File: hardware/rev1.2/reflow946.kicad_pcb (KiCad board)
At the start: 2 copper layers, 104 x 60 mm, 56 parts, among them J1 VH-2A, J2 VH-3A2, J3 VH-3A2, J4 XH-A2, J5 HDR-M-2.54_2x3, Q1 BTA16-600BRG, Q2 MMBT3906, Q3 MMBT3906, Q4 MMBT3906, SW1 SW_Push, SW2 SW_Push, SW3 SW_Push, U1 MOC3041M, U2 ESP32-WROOM-32U, U3 MAX31855KASA, U4 AMS1117-3.3

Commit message: Fork to randware R2 variant
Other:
- board text added: "r2"
- board text added: "randware.us"
- board text removed: "Arnaud Durand"
- board text removed: "r1.2"

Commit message: pcb rev2: place all new parts, TFT alignment silk, pogo-pad J6
- J6: custom 8x SMD pogo-pad array (dia1.6, 2.54 pitch) at bottom strip
  (inside-window THT header rejected: 11.5mm body clashes display glass;
  original location shorted existing segment copper)
- U6/C7/FB3/FB4 probe cluster center field; J7 header top strip;
  J8 EXT_TC terminal bottom-left beside factory probe conn J4
- R21/R22 relocated clear of Reflow946 branding and +3.3V rail track
- Silk: ST7789V3 alignment boxes (32.4x17.3 active / 36x19.3 glass),
  fiducial crosshairs, CC BY 4.0 attribution line
- Zones refilled; DRC vs baseline: zero new electrical/courtyard/mask
  violations; remaining = silk cosmetics + 15 unrouted new-net pads
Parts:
- added C7: 0.01u, C_0805_2012Metric_Pad1.18x1.45mm_HandSolder, F.Cu at (144.0, 105.5)
- added FB3: FerriteBead, R_0603_1608Metric_Pad0.98x0.95mm_HandSolder, F.Cu at (155.5, 103.8)
- added FB4: FerriteBead, R_0603_1608Metric_Pad0.98x0.95mm_HandSolder, F.Cu at (155.5, 107.2)
- added J6: TFT_POGO, , F.Cu at (142.6, 124.3)
- added J7: PROBE_BRK, PinHeader_1x06_P2.54mm_Vertical, F.Cu at (156.0, 74.5)
- added J8: EXT_TC, TerminalBlock_Phoenix_MPT-0,5-2-2.54_1x02_P2.54mm_Horizontal, F.Cu at (108.3, 125.9)
- added R21: 4.7k, R_0603_1608Metric_Pad0.98x0.95mm_HandSolder, F.Cu at (132.5, 119.5)
- added R22: 4.7k, R_0603_1608Metric_Pad0.98x0.95mm_HandSolder, F.Cu at (132.5, 123.2)
- added U6: MAX31855KASA, SOIC-8_3.9x4.9mm_P1.27mm, F.Cu at (150.0, 105.5)
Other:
- board text added: "Based on Reflow946 by A. Durand | CC BY 4.0"
- board text added: "J6"
- board text added: "ST7789V3 ALIGN 32.4x17.3"

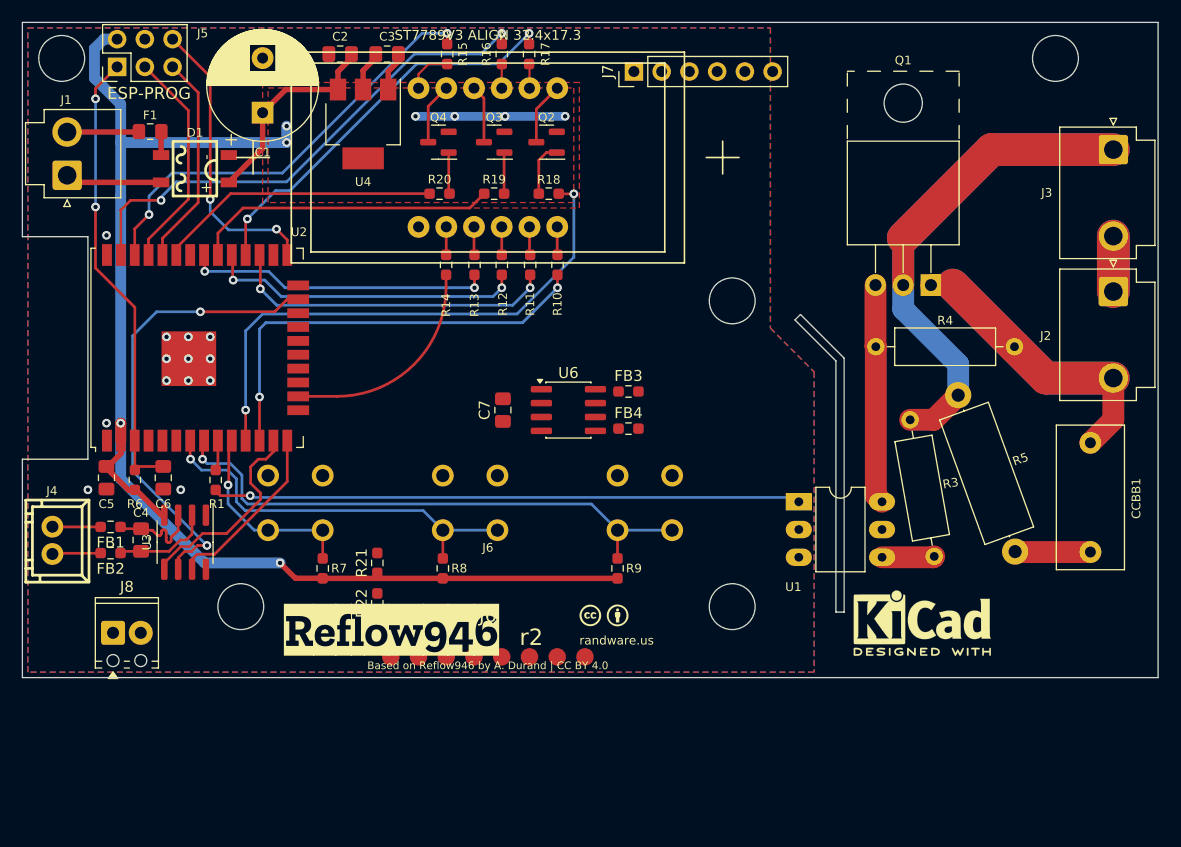
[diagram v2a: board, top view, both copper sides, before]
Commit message: rev2: remove I2C expansion pull-ups R21/R22 (vestigial — display went SPI; IO17/IO22 spare)
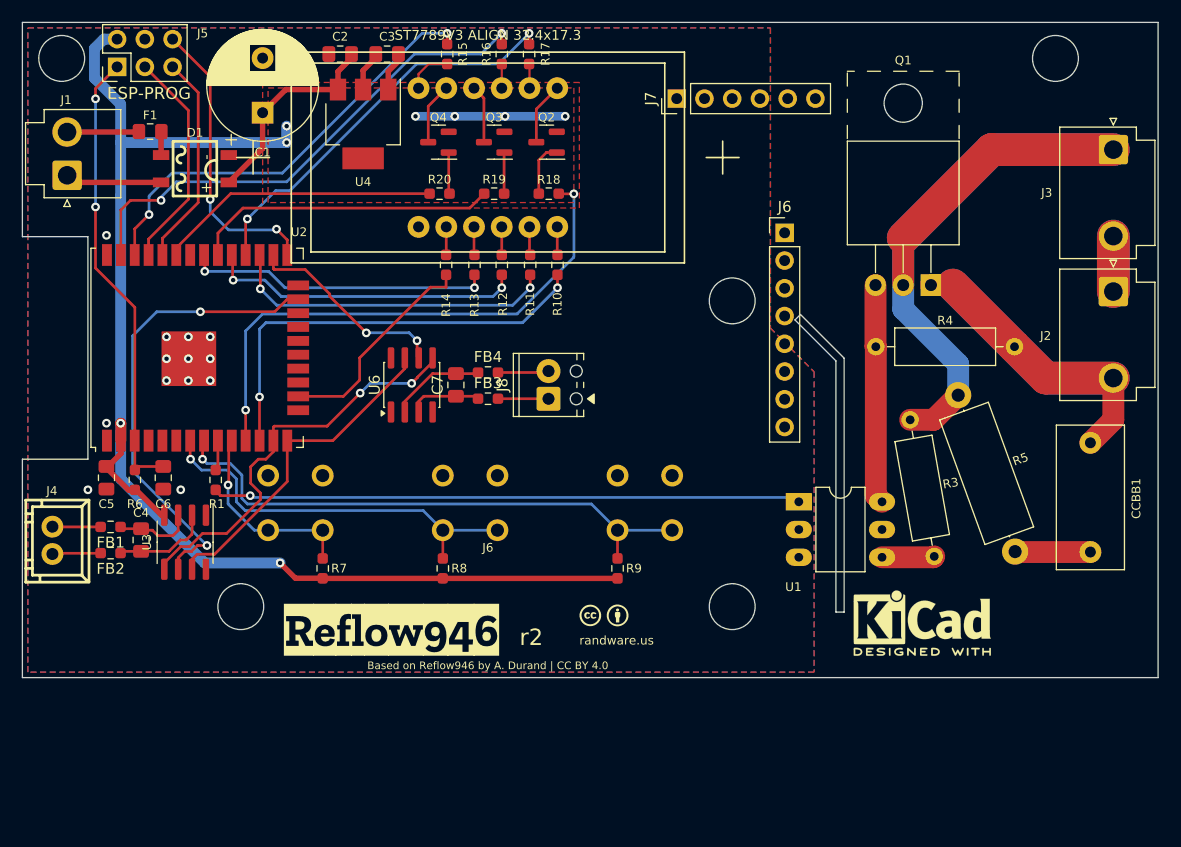
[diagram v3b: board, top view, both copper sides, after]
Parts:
- removed R21, R22: 4.7k, R_0603_1608Metric_Pad0.98x0.95mm_HandSolder
- C7: footprint C_0805_2012Metric_Pad1.18x1.45mm_HandSolder -> Capacitor_SMD:C_0805_2012Metric_Pad1.18x1.45mm_HandSolder
- FB3, FB4: footprint R_0603_1608Metric_Pad0.98x0.95mm_HandSolder -> Resistor_SMD:R_0603_1608Metric_Pad0.98x0.95mm_HandSolder
- J6: value TFT_POGO -> TFT_1.47; footprint (none) -> Connector_PinHeader_2.54mm:PinHeader_1x08_P2.54mm_Vertical
- J7: footprint PinHeader_1x06_P2.54mm_Vertical -> Connector_PinHeader_2.54mm:PinHeader_1x06_P2.54mm_Vertical
- J8: footprint TerminalBlock_Phoenix_MPT-0,5-2-2.54_1x02_P2.54mm_Horizontal -> TerminalBlock_Phoenix:TerminalBlock_Phoenix_MPT-0,5-2-2.54_1x02_P2.54mm_Horizontal
- U6: footprint SOIC-8_3.9x4.9mm_P1.27mm -> Package_SO:SOIC-8_3.9x4.9mm_P1.27mm
- moved J8 45.3 mm to (148.2, 104.5), turned to 90 degrees
- moved J6 44.3 mm to (169.8, 89.3)
- moved U6 14.5 mm to (135.7, 103.2), turned to 90 degrees
- moved FB4 13.9 mm to (142.6, 102.1)
- moved FB3 12.9 mm to (142.6, 104.5)
- moved C7 4.88 mm to (139.7, 103.2)
- moved J7 4.64 mm to (159.9, 77.0)
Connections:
- R11 pad 1: /d -> unconnected-(R11-Pad1)
- R12 pad 1: /dp -> unconnected-(R12-Pad1)
- R13 pad 1: /c -> unconnected-(R13-Pad1)
- R14 pad 1: /g -> unconnected-(R14-Pad1)
- R15 pad 1: /b -> unconnected-(R15-Pad1)
- R16 pad 1: /f -> unconnected-(R16-Pad1)
- R17 pad 1: /a -> unconnected-(R17-Pad1)
- R19 pad 1: /d2 -> unconnected-(R19-Pad1)
- U2 pad 16: /g -> /TFT_RST
- U2 pad 26: unconnected-(U2-IO4-Pad26) -> /CS_EXT
- U2 pad 27: /d -> /TFT_DC
- U2 pad 28: /a -> /SDA
- U2 pad 29: /dp -> /TFT_BLK
- U2 pad 30: /d2 -> /TFT_SCK
- U2 pad 31: /c -> /TFT_MOSI
- U2 pad 36: /b -> /SCL
- U2 pad 37: /f -> /TFT_CS
- U2 pad 4: unconnected-(U2-SENSOR_VP-Pad4) -> /TC_ADC
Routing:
- net (no net): track 0.00 -> 231.8 mm
- net /f: track 46.9 -> 0.00 mm, vias 2 -> 0
- net /b: track 40.4 -> 0.00 mm, vias 2 -> 0
- net /a: track 37.2 -> 0.00 mm, vias 2 -> 0
- net /d: track 30.3 -> 0.00 mm, vias 2 -> 0
- net /dp: track 29.1 -> 0.00 mm, vias 2 -> 0
- net /c: track 28.0 -> 0.00 mm, vias 2 -> 0
- net /d2: track 27.9 -> 0.00 mm
- net /TFT_SCK: track 0.00 -> 27.9 mm
- net /g: track 19.9 -> 0.00 mm
- net /CS_EXT: track 0.00 -> 18.9 mm, vias 0 -> 2
- net /CLK: track 19.0 -> 37.7 mm, vias 0 -> 2
- net /MISO: track 16.5 -> 31.0 mm
- net Net-(U6-T-): track 0.00 -> 8.77 mm
- net Net-(U6-T+): track 0.00 -> 6.69 mm
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
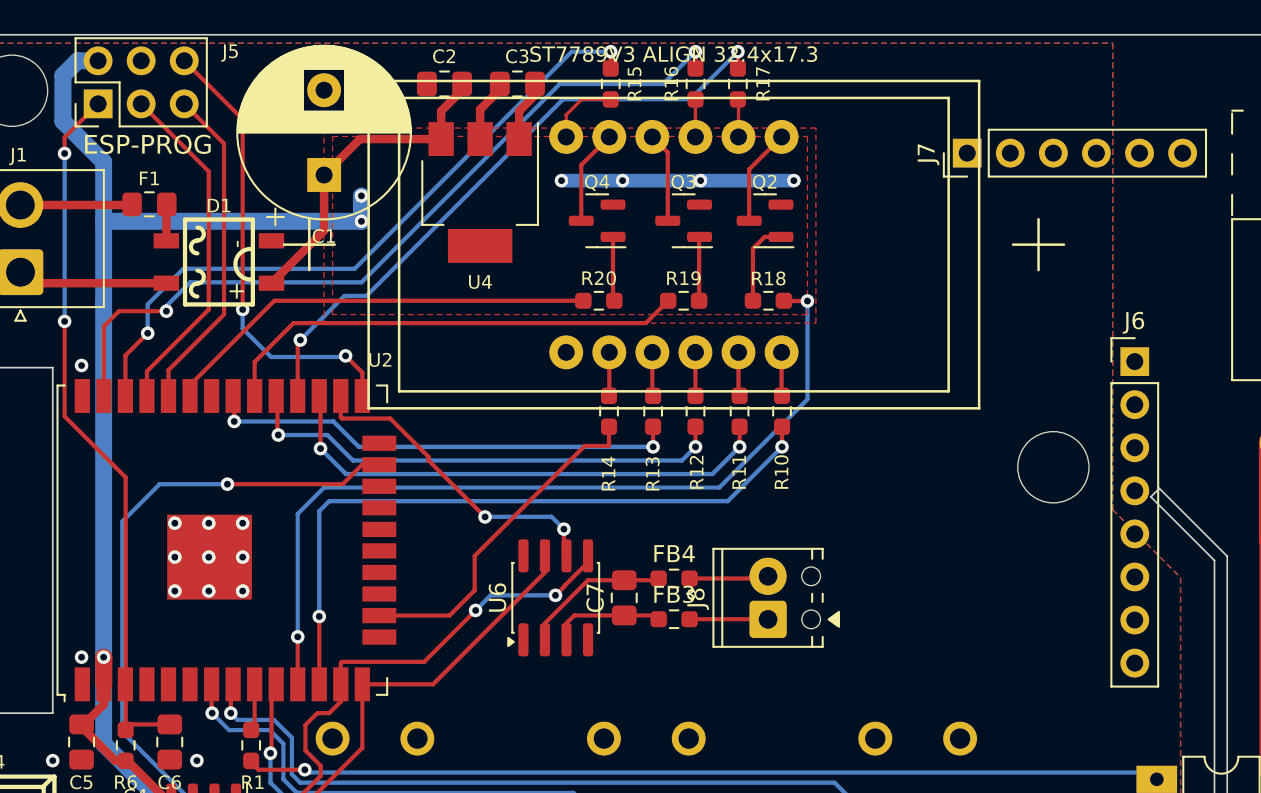
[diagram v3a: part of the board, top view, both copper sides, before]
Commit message: pcb rev2: J6 -> FH12-8S-0.5SH FPC connector; segment drive chain DNP'd; orphan copper swept
- J6 FH12 footprint below alignment window (pogo array retired:
  module is FPC-tail type, confirmed by purchased module pinout)
- R10-R18/R20/Q2/Q4/DS1 marked DNP (7-seg path unsupported since
  segment nets became TFT_*/NC)
- 50 orphaned no-net tracks + 16 stale TFT_* routes removed
- zones refilled
- DRC: zero electrical violations from new placement; remaining =
  user's in-progress probe-cluster routes (8 clip-risks listed) +
  4 conservative J6-vs-cluster courtyards + silk cosmetics
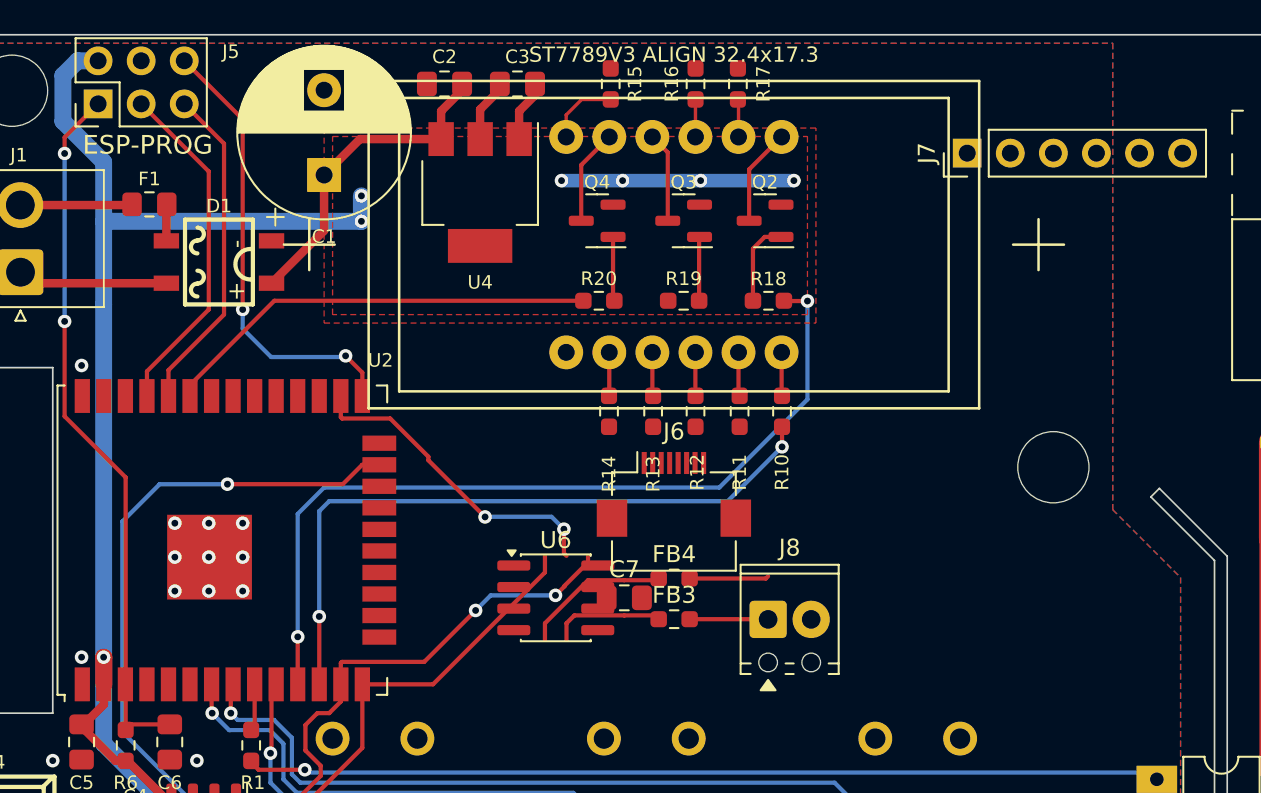
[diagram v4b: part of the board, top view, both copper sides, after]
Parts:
- J6: footprint Connector_PinHeader_2.54mm:PinHeader_1x08_P2.54mm_Vertical -> Hirose_FH12-8S-0.5SH_1x08-1MP_P0.50mm_Horizontal
- moved J6 28.3 mm to (142.6, 97.1)
- turned C7 to 0 degrees
- turned J8 to 0 degrees
- turned U6 to 0 degrees
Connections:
- J6 pad 1: +3.3V -> /TFT_BLK
- J6 pad 2: GND -> /TFT_CS
- J6 pad 3: /TFT_CS -> /TFT_DC
- J6 pad 4: /TFT_DC -> /TFT_RST
- J6 pad 5: /TFT_RST -> /TFT_MOSI
- J6 pad 7: /TFT_MOSI -> +3.3V
- J6 pad 8: /TFT_BLK -> GND
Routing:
- net (no net): track 231.8 -> 0.00 mm
- net /TFT_SCK: track 27.9 -> 0.00 mm
- net /TFT_MOSI: vias 2 -> 0
- net /TFT_DC: vias 2 -> 0
- net /TFT_CS: vias 2 -> 0
- net /TFT_BLK: vias 2 -> 0
- net /SDA: vias 2 -> 0
- net /SCL: vias 2 -> 0

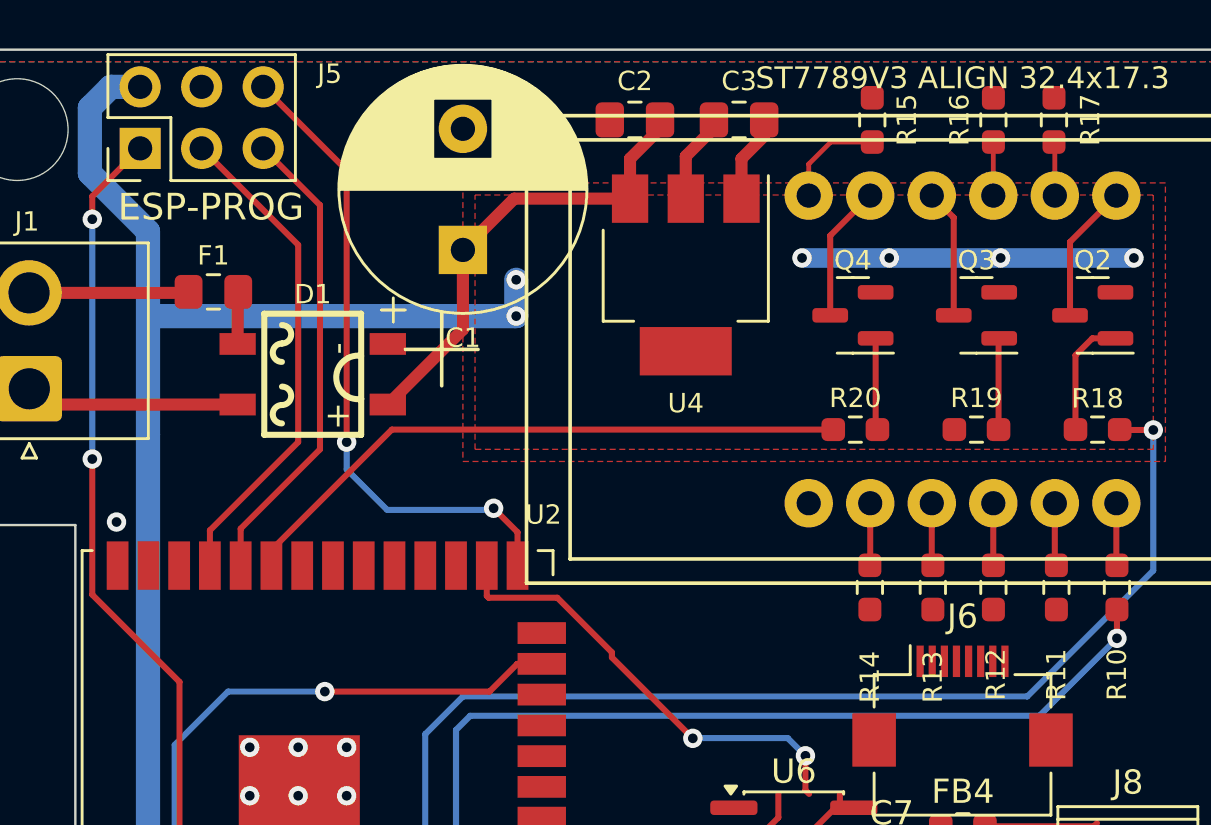
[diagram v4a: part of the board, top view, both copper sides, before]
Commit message: rev2: restore 7-seg plug-and-play path; dual-personality architecture complete
Schematic:
- Segment nets fully restored (a,b,c,d,f,g,dp,d2 DS1-side labels+wires;
  U2-side SDA/SCL/TFT_* reverted to segment names; NC flags removed)
- J6 pins now carry segment nets per FPC tail order:
  1=dp(BL) 2=f(CS) 3=d(DC) 4=g(RES) 5=c(SDA) 6=d2(SCL) 7=+3V3 8=GND
- Segment chain un-DNP'd (DS1, R10-R20, Q2-Q4)

Architecture: one PCB, two personalities via population —
  Board #1: DS1+segment parts fitted, FPC empty -> stock firmware, 7-seg
  Board #2: FPC+display fitted, segment parts out  -> v2 firmware, TFT
(GPIOs shared; mutually exclusive by design)

PCB:
- All pad nets synced to restored netlist (197 updated)
- Original segment routing restored from git history (62 routes)
- Stale orphan copper swept
- DRC: zero electrical violations from restoration; remaining =
  user's in-progress probe-cluster routes + unrouted new nets
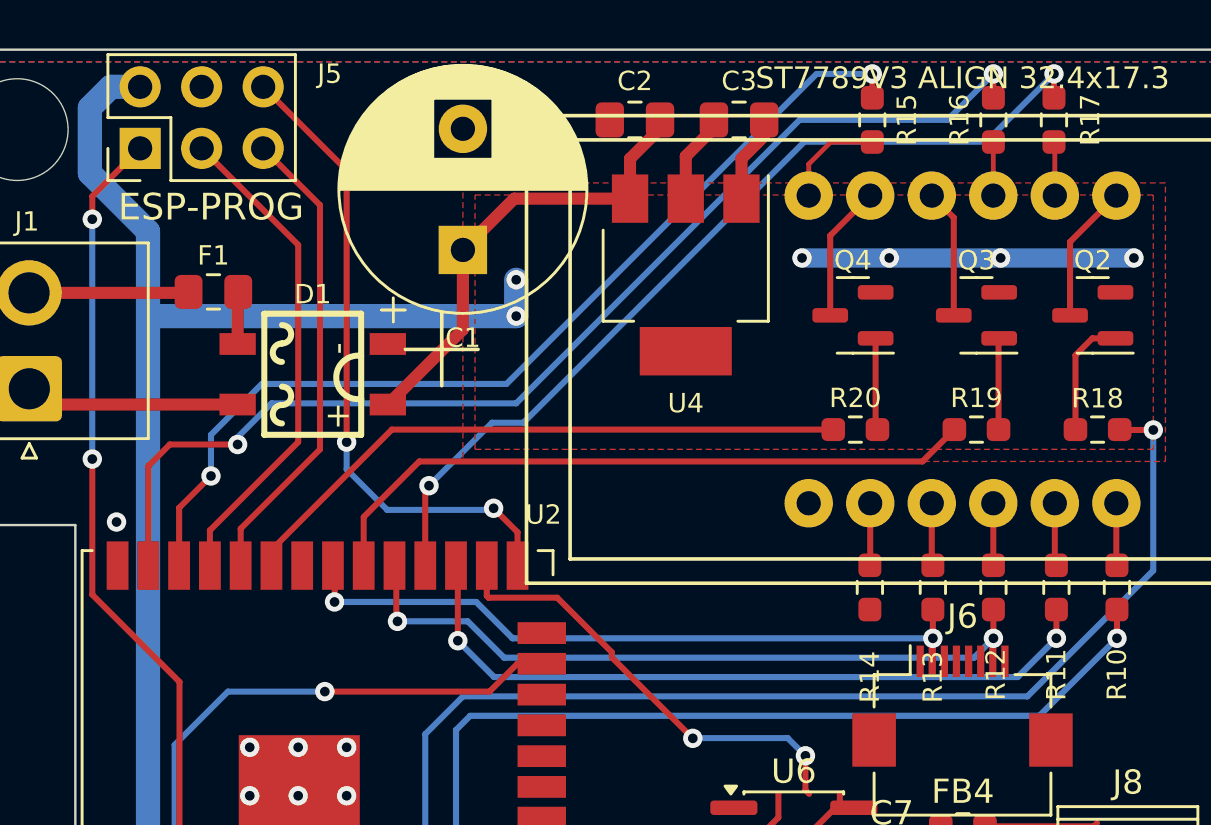
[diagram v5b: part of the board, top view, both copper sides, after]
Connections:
- J6 pad 1: /TFT_BLK -> /dp
- J6 pad 2: /TFT_CS -> /f
- J6 pad 3: /TFT_DC -> /d
- J6 pad 4: /TFT_RST -> /g
- J6 pad 5: /TFT_MOSI -> /c
- J6 pad 6: /TFT_SCK -> /d2
- R11 pad 1: unconnected-(R11-Pad1) -> /d
- R12 pad 1: unconnected-(R12-Pad1) -> /dp
- R13 pad 1: unconnected-(R13-Pad1) -> /c
- R14 pad 1: unconnected-(R14-Pad1) -> /g
- R15 pad 1: unconnected-(R15-Pad1) -> /b
- R16 pad 1: unconnected-(R16-Pad1) -> /f
- R17 pad 1: unconnected-(R17-Pad1) -> /a
- R19 pad 1: unconnected-(R19-Pad1) -> /d2
- U2 pad 16: /TFT_RST -> /g
- U2 pad 27: /TFT_DC -> /d
- U2 pad 28: /SDA -> /a
- U2 pad 29: /TFT_BLK -> /dp
- U2 pad 30: /TFT_SCK -> /d2
- U2 pad 31: /TFT_MOSI -> /c
- U2 pad 36: /SCL -> /b
- U2 pad 37: /TFT_CS -> /f
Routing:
- net /f: track 0.00 -> 46.9 mm, vias 0 -> 2
- net /b: track 0.00 -> 40.4 mm, vias 0 -> 2
- net /a: track 0.00 -> 37.2 mm, vias 0 -> 2
- net /d: track 0.00 -> 30.3 mm, vias 0 -> 2
- net /dp: track 0.00 -> 29.1 mm, vias 0 -> 2
- net /c: track 0.00 -> 28.0 mm, vias 0 -> 2
- net /d2: track 0.00 -> 27.9 mm
